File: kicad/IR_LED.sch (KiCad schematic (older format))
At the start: 5 parts, among them Q2 IRFML8244

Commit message: 新基板，部品を配置
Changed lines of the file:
@@
 AR Path="/57CEFE78/57CF03B8" Ref="Q2"  Part="1"
 AR Path="/57CF2D36/57CF03B8" Ref="Q3"  Part="1"
-F 0 "Q2" H 6100 4850 50  0000 R CNN
+F 0 "Q3" H 6100 4850 50  0000 R CNN
 F 1 "IRFML8244" H 6450 4750 50  0000 R CNN
 F 2 "TO_SOT_Packages_SMD:SOT-23" H 6000 4900 50  0001 C CNN
@@
 AR Path="/57CEFE78/57CF03DE" Ref="D3"  Part="1"
 AR Path="/57CF2D36/57CF03DE" Ref="D9"  Part="1"
-F 0 "D3" H 5900 3800 50  0000 C CNN
+F 0 "D9" H 5900 3800 50  0000 C CNN
 F 1 "VSLY5850" H 5900 3600 50  0000 C CNN
 F 2 "mouse:LED-5MM_Angle" H 5900 3700 50  0001 C CNN
@@
 AR Path="/57CEFE78/5836B55A" Ref="R6"  Part="1"
 AR Path="/57CF2D36/5836B55A" Ref="R16"  Part="1"
-F 0 "R6" V 5980 4250 50  0000 C CNN
+F 0 "R16" V 5980 4250 50  0000 C CNN
 F 1 "15" V 5900 4250 50  0000 C CNN
 F 2 "Resistors_SMD:R_0805" V 5830 4250 50  0001 C CNN
@@
 AR Path="/57CEFE78/5836B8B1" Ref="D2"  Part="1"
 AR Path="/57CF2D36/5836B8B1" Ref="D8"  Part="1"
-F 0 "D2" H 5900 3200 50  0000 C CNN
+F 0 "D8" H 5900 3200 50  0000 C CNN
 F 1 "VSLY5850" H 5900 3000 50  0000 C CNN
 F 2 "mouse:LED-5MM_Angle" H 5900 3100 50  0001 C CNN
@@
 AR Path="/57CEFE78/5836B959" Ref="R7"  Part="1"
 AR Path="/57CF2D36/5836B959" Ref="R17"  Part="1"
-F 0 "R7" V 5580 5050 50  0000 C CNN
+F 0 "R17" V 5580 5050 50  0000 C CNN
 F 1 "10k" V 5500 5050 50  0000 C CNN
 F 2 "Resistors_SMD:R_0402" V 5430 5050 50  0001 C CNN

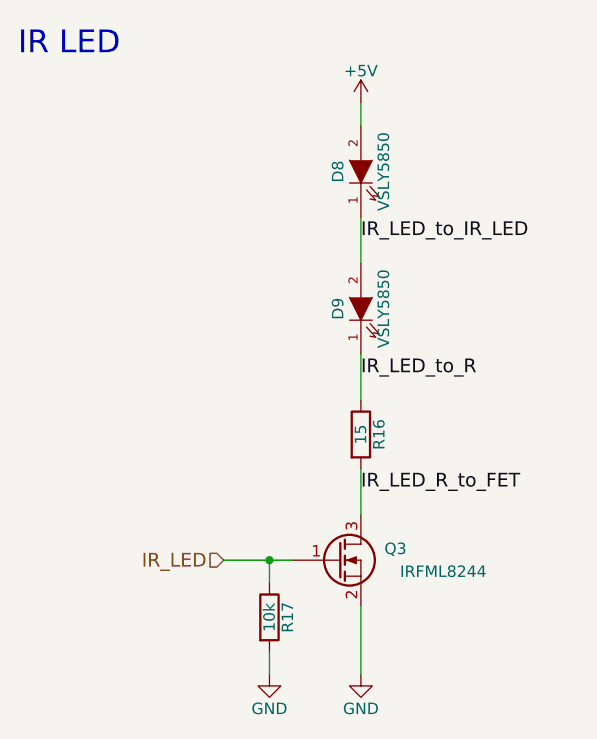
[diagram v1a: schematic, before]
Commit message: 自動配線用にdsn吐き出し
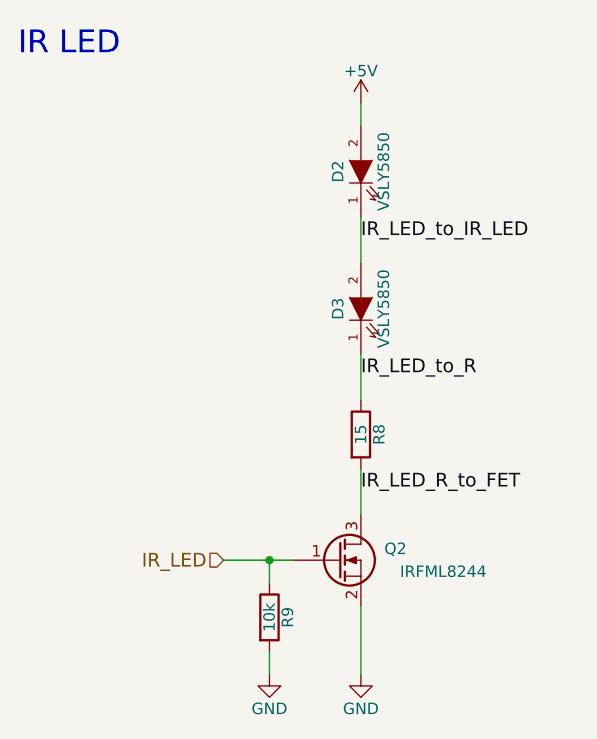
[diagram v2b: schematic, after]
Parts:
- D2: footprint mouse:LED-5MM_Angle -> mouse:LED-5MM_Angle_wide
- renumbered R6 to R8, R7 to R9
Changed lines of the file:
@@
 $Descr A4 11693 8268
 encoding utf-8
-Sheet 5 15
+Sheet 10 15
 Title ""
 Date ""
@@
 AR Path="/57CEFE78/57CF03B8" Ref="Q2"  Part="1"
 AR Path="/57CF2D36/57CF03B8" Ref="Q3"  Part="1"
-F 0 "Q3" H 6100 4850 50  0000 R CNN
+F 0 "Q2" H 6100 4850 50  0000 R CNN
 F 1 "IRFML8244" H 6450 4750 50  0000 R CNN
 F 2 "TO_SOT_Packages_SMD:SOT-23" H 6000 4900 50  0001 C CNN
@@
 $EndComp
 $Comp
-L GND #PWR059
+L GND #PWR055
 U 1 1 57CF03C0
 P 5900 5300
-AR Path="/57CEFE78/57CF03C0" Ref="#PWR059"  Part="1"
-AR Path="/57CF2D36/57CF03C0" Ref="#PWR082"  Part="1"
-F 0 "#PWR082" H 5900 5050 50  0001 C CNN
+AR Path="/57CEFE78/57CF03C0" Ref="#PWR055"  Part="1"
+AR Path="/57CF2D36/57CF03C0" Ref="#PWR078"  Part="1"
+F 0 "#PWR078" H 5900 5050 50  0001 C CNN
 F 1 "GND" H 5900 5150 50  0000 C CNN
 F 2 "" H 5900 5300 50  0000 C CNN
@@
 AR Path="/57CEFE78/57CF03DE" Ref="D3"  Part="1"
 AR Path="/57CF2D36/57CF03DE" Ref="D9"  Part="1"
-F 0 "D9" H 5900 3800 50  0000 C CNN
+F 0 "D3" H 5900 3800 50  0000 C CNN
 F 1 "VSLY5850" H 5900 3600 50  0000 C CNN
 F 2 "mouse:LED-5MM_Angle" H 5900 3700 50  0001 C CNN
@@
 IR LED
 $Comp
-L R R6
+L R R8
 U 1 1 5836B55A
 P 5900 4250
-AR Path="/57CEFE78/5836B55A" Ref="R6"  Part="1"
-AR Path="/57CF2D36/5836B55A" Ref="R16"  Part="1"
-F 0 "R16" V 5980 4250 50  0000 C CNN
+AR Path="/57CEFE78/5836B55A" Ref="R8"  Part="1"
+AR Path="/57CF2D36/5836B55A" Ref="R18"  Part="1"
+F 0 "R8" V 5980 4250 50  0000 C CNN
 F 1 "15" V 5900 4250 50  0000 C CNN
 F 2 "Resistors_SMD:R_0805" V 5830 4250 50  0001 C CNN
@@
 	5900 4100 5900 3900
 $Comp
-L +5V #PWR060
+L +5V #PWR056
 U 1 1 5836B893
 P 5900 2800
-AR Path="/57CEFE78/5836B893" Ref="#PWR060"  Part="1"
-AR Path="/57CF2D36/5836B893" Ref="#PWR083"  Part="1"
-F 0 "#PWR083" H 5900 2650 50  0001 C CNN
+AR Path="/57CEFE78/5836B893" Ref="#PWR056"  Part="1"
+AR Path="/57CF2D36/5836B893" Ref="#PWR079"  Part="1"
+F 0 "#PWR079" H 5900 2650 50  0001 C CNN
 F 1 "+5V" H 5900 2940 50  0000 C CNN
 F 2 "" H 5900 2800 50  0000 C CNN
@@
 AR Path="/57CEFE78/5836B8B1" Ref="D2"  Part="1"
 AR Path="/57CF2D36/5836B8B1" Ref="D8"  Part="1"
-F 0 "D8" H 5900 3200 50  0000 C CNN
+F 0 "D2" H 5900 3200 50  0000 C CNN
 F 1 "VSLY5850" H 5900 3000 50  0000 C CNN
-F 2 "mouse:LED-5MM_Angle" H 5900 3100 50  0001 C CNN
+F 2 "mouse:LED-5MM_Angle_wide" H 5900 3100 50  0001 C CNN
 F 3 "" H 5900 3100 50  0000 C CNN
 	1    5900 3100
@@
 IR_LED_to_IR_LED
 $Comp
-L R R7
+L R R9
 U 1 1 5836B959
 P 5500 5050
-AR Path="/57CEFE78/5836B959" Ref="R7"  Part="1"
-AR Path="/57CF2D36/5836B959" Ref="R17"  Part="1"
-F 0 "R17" V 5580 5050 50  0000 C CNN
+AR Path="/57CEFE78/5836B959" Ref="R9"  Part="1"
+AR Path="/57CF2D36/5836B959" Ref="R19"  Part="1"
+F 0 "R9" V 5580 5050 50  0000 C CNN
 F 1 "10k" V 5500 5050 50  0000 C CNN
 F 2 "Resistors_SMD:R_0402" V 5430 5050 50  0001 C CNN
@@
 Connection ~ 5500 4800
 $Comp
-L GND #PWR061
+L GND #PWR057
 U 1 1 5836B9AB
 P 5500 5300
-AR Path="/57CEFE78/5836B9AB" Ref="#PWR061"  Part="1"
-AR Path="/57CF2D36/5836B9AB" Ref="#PWR084"  Part="1"
-F 0 "#PWR084" H 5500 5050 50  0001 C CNN
+AR Path="/57CEFE78/5836B9AB" Ref="#PWR057"  Part="1"
+AR Path="/57CF2D36/5836B9AB" Ref="#PWR080"  Part="1"
+F 0 "#PWR080" H 5500 5050 50  0001 C CNN
 F 1 "GND" H 5500 5150 50  0000 C CNN
 F 2 "" H 5500 5300 50  0000 C CNN
